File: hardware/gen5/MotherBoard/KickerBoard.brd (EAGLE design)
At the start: 141.6 x 142.1 mm, 156 parts, among them U1 SAM3S4B

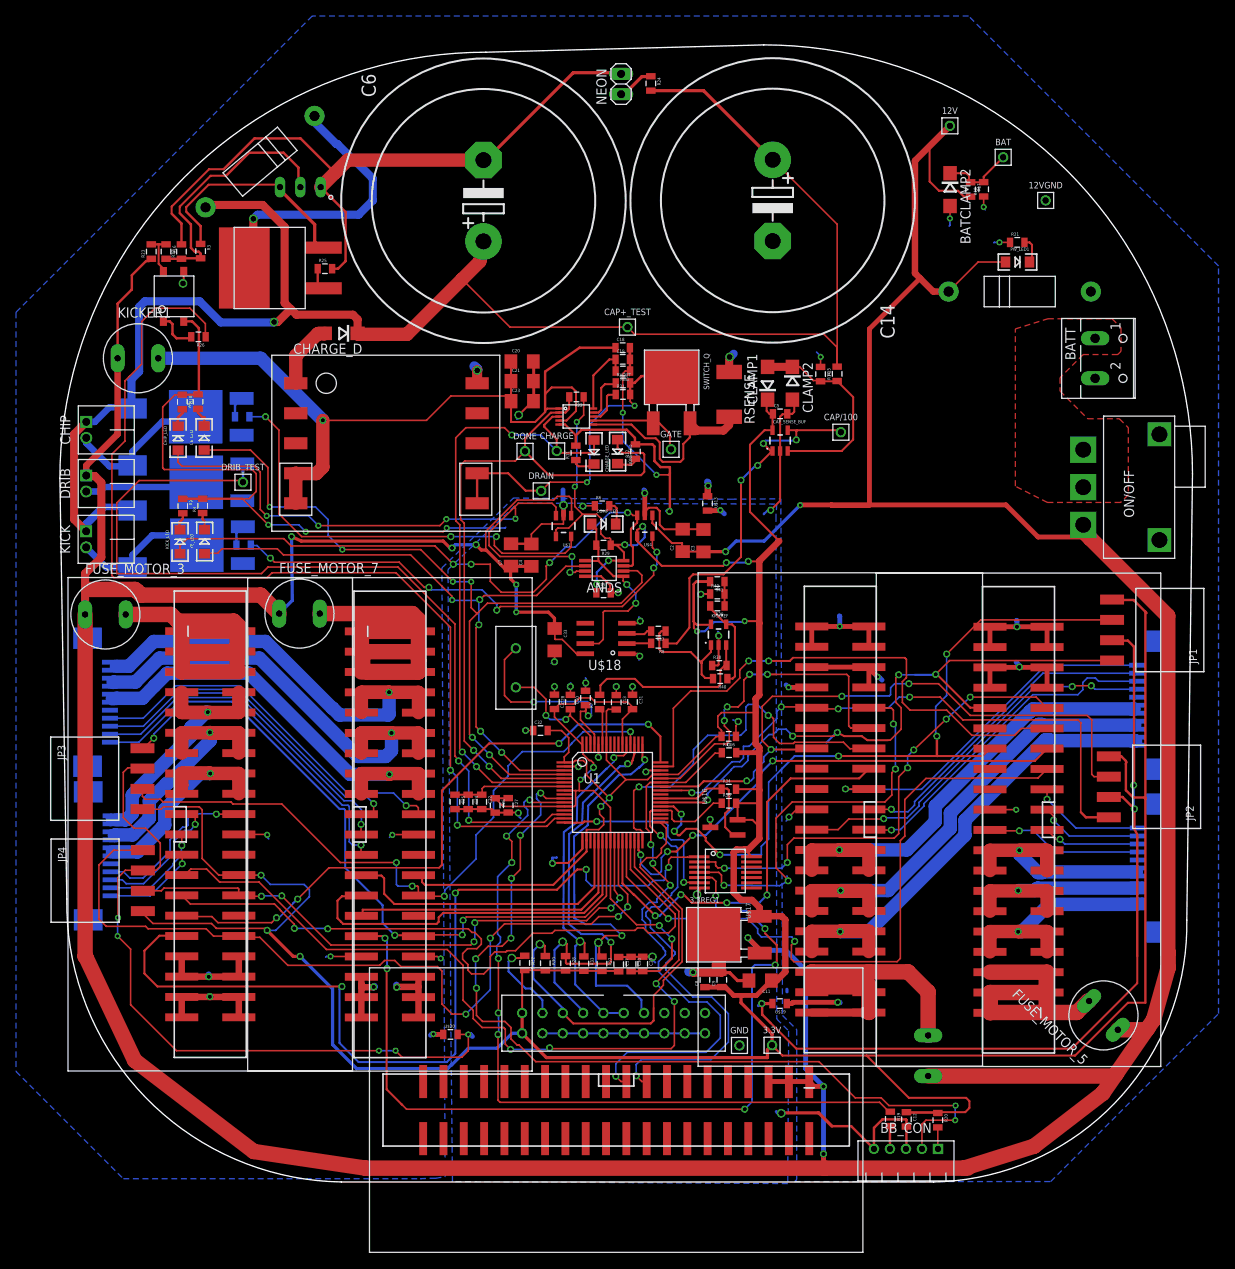
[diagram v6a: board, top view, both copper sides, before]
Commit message: Working through DRC Errors. Need to look into tolerances of PCB fab.
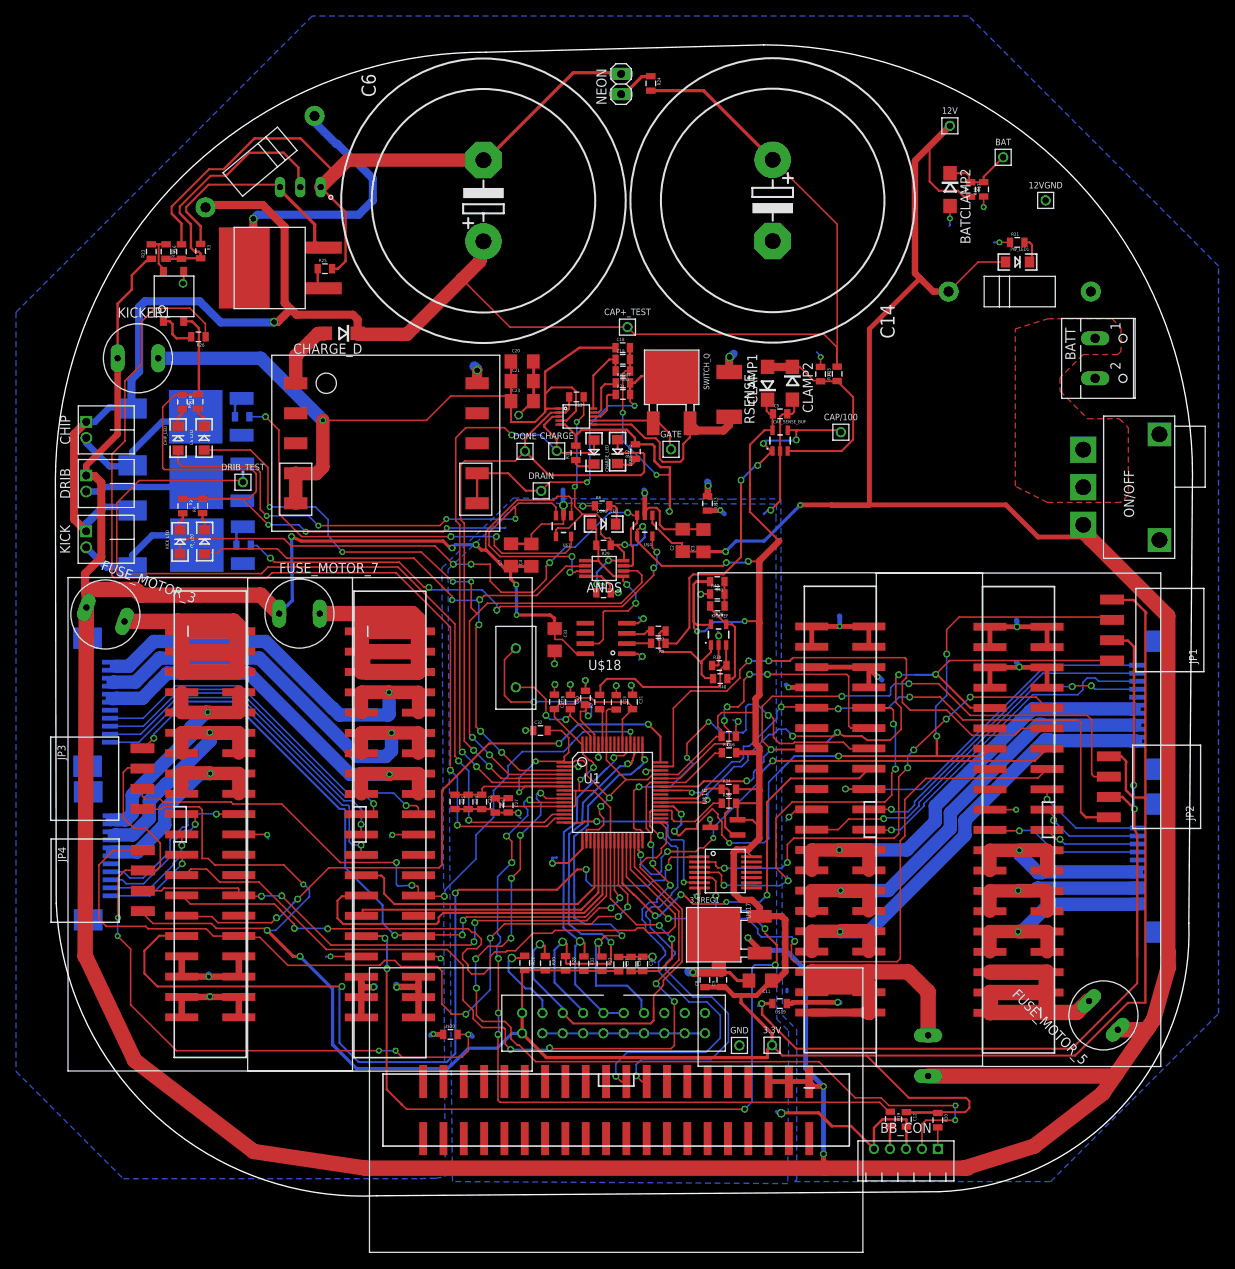
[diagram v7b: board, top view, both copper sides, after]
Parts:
- turned FUSE_MOTOR_3 to 340 degrees
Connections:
- removed net N$34: C22.1, C24.1, C25.1, U1.7
- net 3.3V: now also C22.1, C24.1, C25.1, U1.7
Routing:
- net N$34: track 14.5 -> 0.00 mm
- net 3.3V: track 588.4 -> 593.0 mm, vias 15 -> 17
- net M1QA-2: track 93.2 -> 96.9 mm
- net BREN2: track 47.5 -> 50.2 mm, vias 2 -> 4
- net GND: track 472.4 -> 474.2 mm
- net BREN1: track 62.4 -> 63.2 mm
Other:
- board size 141.6 x 142.1 mm -> 142.1 x 143.9 mm

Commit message: fixed clearance issues. all traces at least separated by 8 mils
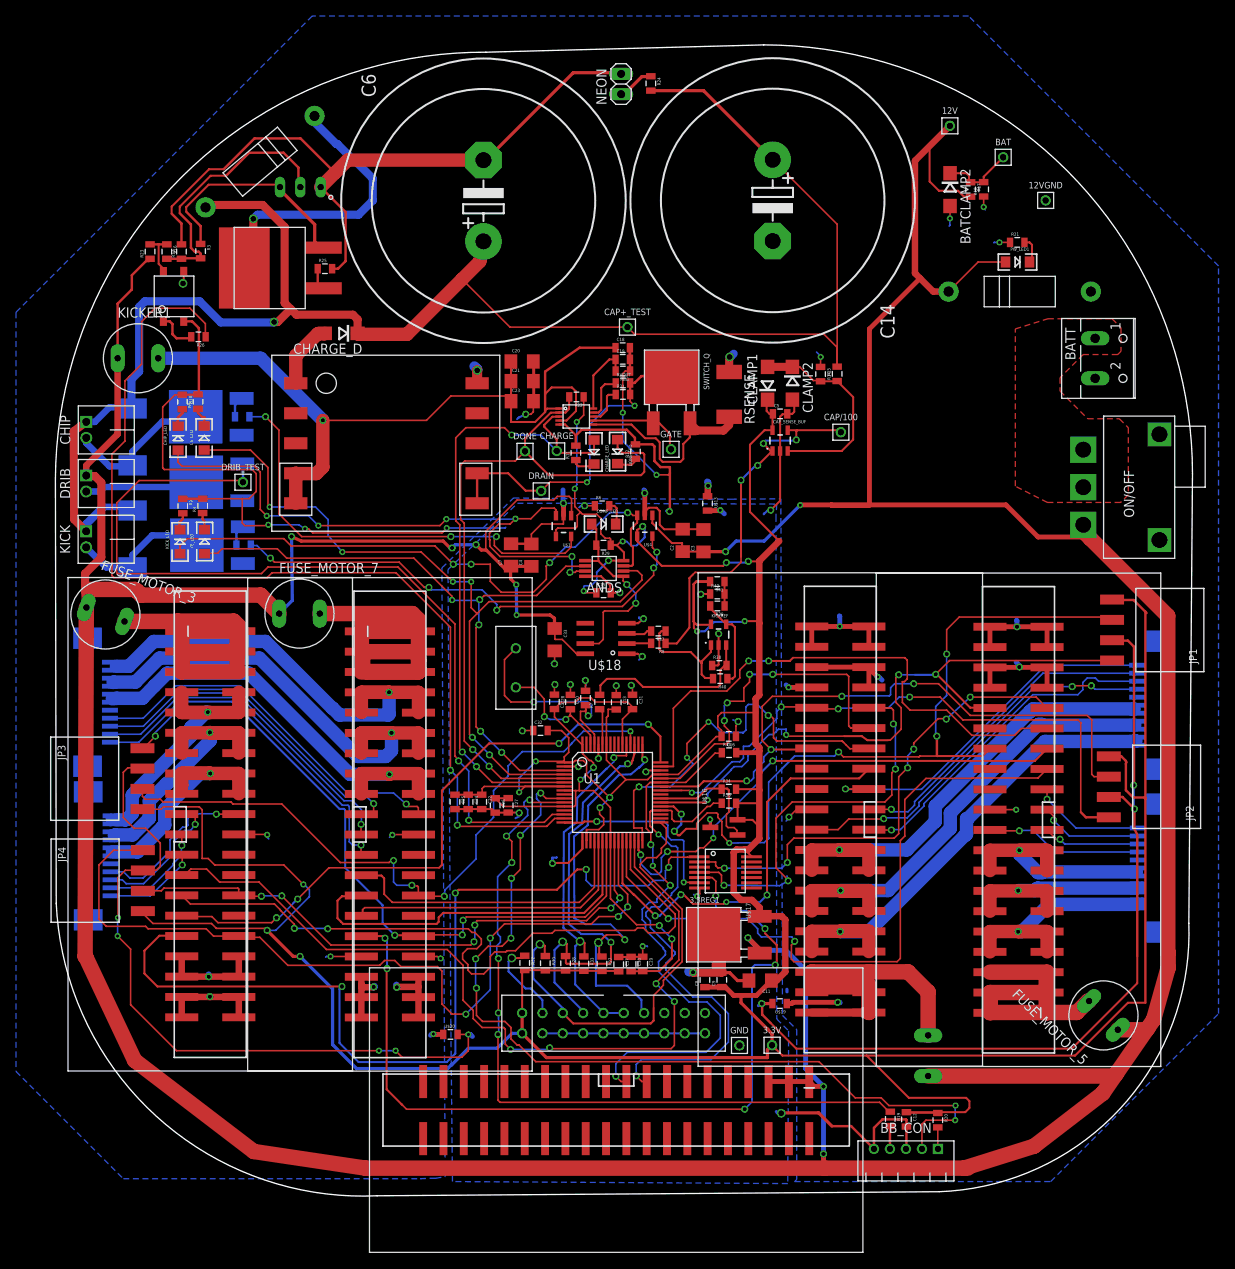
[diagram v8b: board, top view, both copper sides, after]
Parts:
- moved R23 0.15 mm to (10.4, 115.2)
- moved R16 0.10 mm to (12.5, 115.2)
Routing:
- net 3.3V: track 593.0 -> 596.6 mm
- net M1QB-2: track 85.9 -> 83.5 mm, vias 5 -> 4
- net AND_CHIP: track 79.4 -> 77.1 mm
- net TDO: track 52.4 -> 53.7 mm
- net GND: track 474.2 -> 473.2 mm
- net 12VGND: track 273.2 -> 274.0 mm
- net FAULT1: track 60.0 -> 60.5 mm
- net N$33: track 16.0 -> 16.6 mm
